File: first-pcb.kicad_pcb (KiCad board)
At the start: 2 copper layers, 88.9 x 45.7 mm, 8 parts, among them K1 my_connector, P1 10k, Q1 BC547, U1 LM358

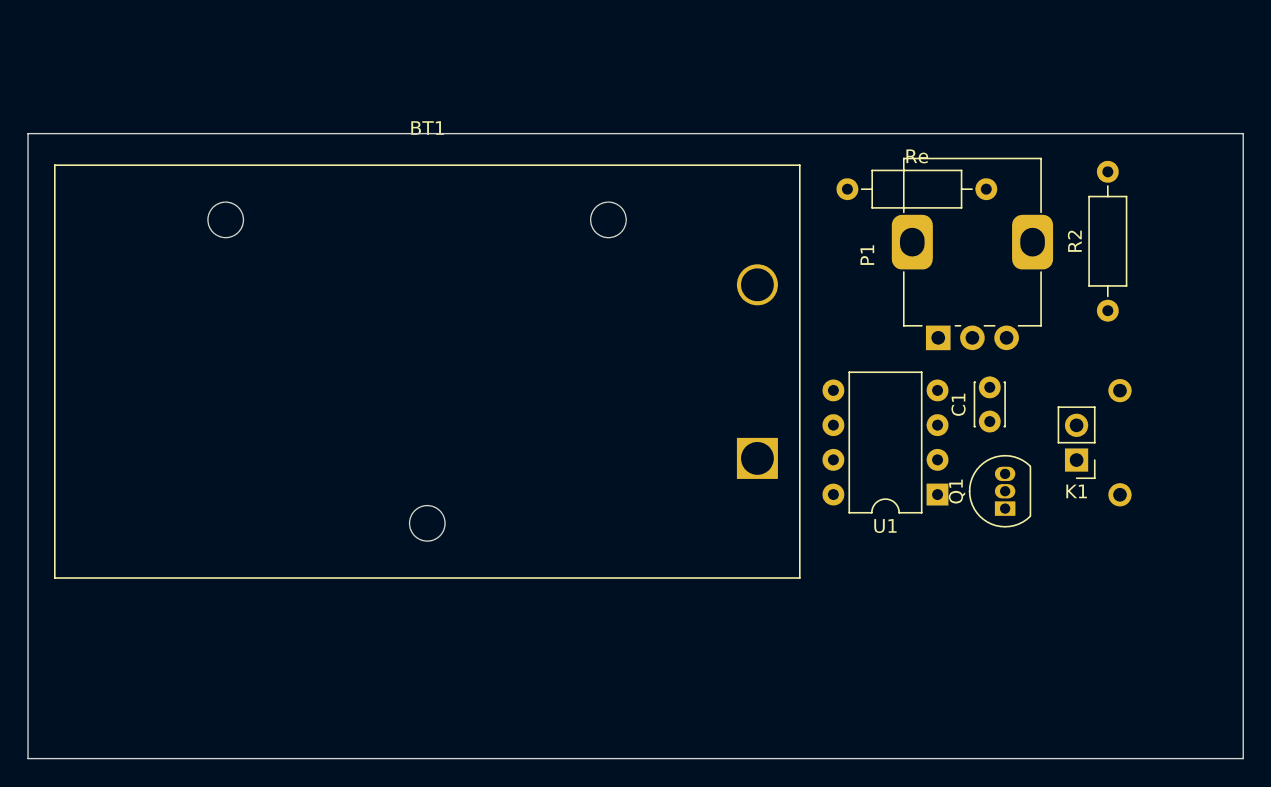
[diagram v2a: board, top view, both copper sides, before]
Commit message: Adding Grounding Holes to pcb
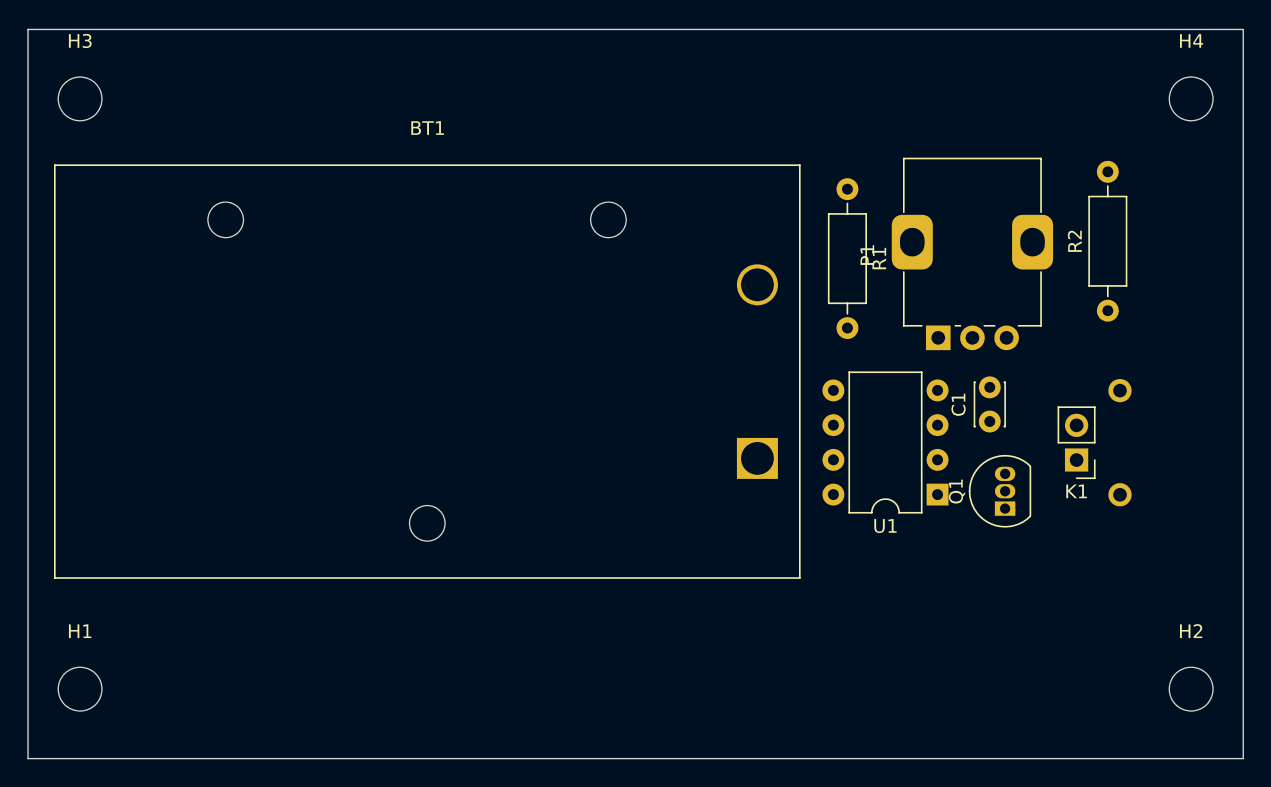
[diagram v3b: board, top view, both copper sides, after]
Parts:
- added H1: MountingHole_Pad, MountingHole:MountingHole_3.2mm_M3, F.Cu at (86.4, 119.4)
- added H2: MountingHole_Pad, MountingHole:MountingHole_3.2mm_M3, F.Cu at (167.6, 119.4)
- added H3: MountingHole_Pad, MountingHole:MountingHole_3.2mm_M3, F.Cu at (86.4, 76.2)
- added H4: MountingHole_Pad, MountingHole:MountingHole_3.2mm_M3, F.Cu at (167.6, 76.2)
- turned R1 to -90 degrees
- renumbered Re to R1
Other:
- board size 88.9 x 45.7 mm -> 88.9 x 53.3 mm
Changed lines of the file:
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@@
   (net 4 "GND")
   (net 5 "Net-(C1-Pad1)")
-  (net 6 "Net-(U1-Pad1)")
-  (net 7 "Net-(K1-Pad1)")
-  (net 8 "unconnected-(U1-Pad5)")
-  (net 9 "unconnected-(U1-Pad6)")
-  (net 10 "unconnected-(U1-Pad7)")
+  (net 6 "Net-(K1-Pad1)")
+  (net 7 "unconnected-(U1-Pad5)")
+  (net 8 "unconnected-(U1-Pad6)")
+  (net 9 "unconnected-(U1-Pad7)")
+  (net 10 "Net-(Q1-Pad2)")
   (footprint "Potentiometer_THT:Potentiometer_Alps_RK09K_Single_Vertical" (layer "F.Cu")
     (at 149.138 93.68 90)
@@
     (fp_line (start 6.985 8.89) (end 0.635 8.89) (layer "F.Fab") (width 0.1))
     (pad "1" thru_hole rect (at 0 0 180) (size 1.6 1.6) (drill 0.8) (layers *.Cu *.Mask)
-      (net 6 "Net-(U1-Pad1)") (pintype "output"))
+      (net 10 "Net-(Q1-Pad2)") (pintype "output"))
     (pad "2" thru_hole oval (at 0 2.54 180) (size 1.6 1.6) (drill 0.8) (layers *.Cu *.Mask)
-      (net 7 "Net-(K1-Pad1)") (pinfunction "-") (pintype "input"))
+      (net 6 "Net-(K1-Pad1)") (pinfunction "-") (pintype "input"))
     (pad "3" thru_hole oval (at 0 5.08 180) (size 1.6 1.6) (drill 0.8) (layers *.Cu *.Mask)
       (net 5 "Net-(C1-Pad1)") (pinfunction "+") (pintype "input"))
@@
       (net 4 "GND") (pinfunction "V-") (pintype "power_in"))
     (pad "5" thru_hole oval (at 7.62 7.62 180) (size 1.6 1.6) (drill 0.8) (layers *.Cu *.Mask)
-      (net 8 "unconnected-(U1-Pad5)") (pinfunction "+") (pintype "input+no_connect"))
+      (net 7 "unconnected-(U1-Pad5)") (pinfunction "+") (pintype "input+no_connect"))
     (pad "6" thru_hole oval (at 7.62 5.08 180) (size 1.6 1.6) (drill 0.8) (layers *.Cu *.Mask)
-      (net 9 "unconnected-(U1-Pad6)") (pinfunction "-") (pintype "input+no_connect"))
+      (net 8 "unconnected-(U1-Pad6)") (pinfunction "-") (pintype "input+no_connect"))
     (pad "7" thru_hole oval (at 7.62 2.54 180) (size 1.6 1.6) (drill 0.8) (layers *.Cu *.Mask)
-      (net 10 "unconnected-(U1-Pad7)") (pintype "output+no_connect"))
+      (net 9 "unconnected-(U1-Pad7)") (pintype "output+no_connect"))
     (pad "8" thru_hole oval (at 7.62 0 180) (size 1.6 1.6) (drill 0.8) (layers *.Cu *.Mask)
       (net 1 "Net-(BT1-Pad1)") (pinfunction "V+") (pintype "power_in"))
@@
       (rotate (xyz 0 0 0))
     )
+  )
+  (footprint "MountingHole:MountingHole_3.2mm_M3" (layer "F.Cu")
+    (at 86.36 76.2)
+    (descr "Mounting Hole 3.2mm, no annular, M3")
+    (tags "mounting hole 3.2mm no annular m3")
+    (property "Sheetfile" "first-pcb.kicad_sch")
+    (property "Sheetname" "")
+    (attr exclude_from_pos_files)
+    (fp_text reference "H3" (at 0 -4.2) (layer "F.SilkS")
+      (effects (font (size 1 1) (thickness 0.15)))
+    )
+    (fp_text value "MountingHole_Pad" (at 0 4.2) (layer "F.Fab")
+      (effects (font (size 1 1) (thickness 0.15)))
+    )
+    (fp_text user "${REFERENCE}" (at 0 0) (layer "F.Fab")
+      (effects (font (size 1 1) (thickness 0.15)))
+    )
+    (fp_circle (center 0 0) (end 3.2 0) (layer "Cmts.User") (width 0.15) (fill none))
+    (fp_circle (center 0 0) (end 3.45 0) (layer "F.CrtYd") (width 0.05) (fill none))
+    (pad "" np_thru_hole circle (at 0 0) (size 3.2 3.2) (drill 3.2) (layers *.Cu *.Mask))
+  )
+  (footprint "MountingHole:MountingHole_3.2mm_M3" (layer "F.Cu")
+    (at 86.36 119.38)
+    (descr "Mounting Hole 3.2mm, no annular, M3")
+    (tags "mounting hole 3.2mm no annular m3")
+    (property "Sheetfile" "first-pcb.kicad_sch")
+    (property "Sheetname" "")
+    (attr exclude_from_pos_files)
+    (fp_text reference "H1" (at 0 -4.2) (layer "F.SilkS")
+      (effects (font (size 1 1) (thickness 0.15)))
+    )
+    (fp_text value "MountingHole_Pad" (at 0 4.2) (layer "F.Fab")
+      (effects (font (size 1 1) (thickness 0.15)))
+    )
+    (fp_text user "${REFERENCE}" (at 0 0) (layer "F.Fab")
+      (effects (font (size 1 1) (thickness 0.15)))
+    )
+    (fp_circle (center 0 0) (end 3.2 0) (layer "Cmts.User") (width 0.15) (fill none))
+    (fp_circle (center 0 0) (end 3.45 0) (layer "F.CrtYd") (width 0.05) (fill none))
+    (pad "" np_thru_hole circle (at 0 0) (size 3.2 3.2) (drill 3.2) (layers *.Cu *.Mask))
   )
   (footprint "Battery:BatteryHolder_Eagle_12BH611-GR" (layer "F.Cu")
@@
       (net 1 "Net-(BT1-Pad1)") (pinfunction "C") (pintype "passive"))
     (pad "2" thru_hole oval (at 1.27 0 90) (size 1.05 1.5) (drill 0.75) (layers *.Cu *.Mask)
-      (net 6 "Net-(U1-Pad1)") (pinfunction "B") (pintype "input"))
+      (net 10 "Net-(Q1-Pad2)") (pinfunction "B") (pintype "input"))
     (pad "3" thru_hole oval (at 2.54 0 90) (size 1.05 1.5) (drill 0.75) (layers *.Cu *.Mask)
-      (net 7 "Net-(K1-Pad1)") (pinfunction "E") (pintype "passive"))
+      (net 6 "Net-(K1-Pad1)") (pinfunction "E") (pintype "passive"))
     (model "${KICAD6_3DMODEL_DIR}/Package_TO_SOT_THT.3dshapes/TO-92_Inline.wrl"
       (offset (xyz 0 0 0))
@@
   )
   (footprint "Resistor_THT:R_Axial_DIN0207_L6.3mm_D2.5mm_P10.16mm_Horizontal" (layer "F.Cu")
-    (at 142.494 82.804)
+    (at 142.494 82.804 -90)
     (descr "Resistor, Axial_DIN0207 series, Axial, Horizontal, pin pitch=10.16mm, 0.25W = 1/4W, length*diameter=6.3*2.5mm^2, http://cdn-reichelt.de/documents/datenblatt/B400/1_4W%23YAG.pdf")
     (tags "Resistor Axial_DIN0207 series Axial Horizontal pin pitch 10.16mm 0.25W = 1/4W length 6.3mm diameter 2.5mm")
@@
     (property "Sheetname" "")
     (attr through_hole)
-    (fp_text reference "Re" (at 5.08 -2.37) (layer "F.SilkS")
-      (effects (font (size 1 1) (thickness 0.15)))
-    )
-    (fp_text value "100R" (at 5.08 2.37) (layer "F.Fab")
-      (effects (font (size 1 1) (thickness 0.15)))
-    )
-    (fp_text user "${REFERENCE}" (at 5.08 0) (layer "F.Fab")
+    (fp_text reference "R1" (at 5.08 -2.37 90) (layer "F.SilkS")
+      (effects (font (size 1 1) (thickness 0.15)))
+    )
+    (fp_text value "100R" (at 5.08 2.37 90) (layer "F.Fab")
+      (effects (font (size 1 1) (thickness 0.15)))
+    )
+    (fp_text user "${REFERENCE}" (at 5.08 0 90) (layer "F.Fab")
       (effects (font (size 1 1) (thickness 0.15)))
     )
@@
     (fp_line (start 8.23 1.25) (end 8.23 -1.25) (layer "F.Fab") (width 0.1))
     (fp_line (start 1.93 1.25) (end 8.23 1.25) (layer "F.Fab") (width 0.1))
-    (pad "1" thru_hole circle (at 0 0) (size 1.6 1.6) (drill 0.8) (layers *.Cu *.Mask)
+    (pad "1" thru_hole circle (at 0 0 270) (size 1.6 1.6) (drill 0.8) (layers *.Cu *.Mask)
       (net 1 "Net-(BT1-Pad1)") (pintype "passive"))
-    (pad "2" thru_hole oval (at 10.16 0) (size 1.6 1.6) (drill 0.8) (layers *.Cu *.Mask)
+    (pad "2" thru_hole oval (at 10.16 0 270) (size 1.6 1.6) (drill 0.8) (layers *.Cu *.Mask)
       (net 2 "Net-(P1-Pad1)") (pintype "passive"))
     (model "${KICAD6_3DMODEL_DIR}/Resistor_THT.3dshapes/R_Axial_DIN0207_L6.3mm_D2.5mm_P10.16mm_Horizontal.wrl"
@@
     (fp_line (start -1.27 -0.635) (end -0.635 -1.27) (layer "F.Fab") (width 0.1))
     (pad "1" thru_hole rect (at 0 0 180) (size 1.7 1.7) (drill 1) (layers *.Cu *.Mask)
-      (net 7 "Net-(K1-Pad1)") (pintype "input"))
+      (net 6 "Net-(K1-Pad1)") (pintype "input"))
     (pad "2" thru_hole circle (at 0 2.54 180) (size 1.7 1.7) (drill 1) (layers *.Cu *.Mask)
       (net 4 "GND") (pintype "input"))
@@
       (rotate (xyz 0 0 0))
     )
+  )
+  (footprint "MountingHole:MountingHole_3.2mm_M3" (layer "F.Cu")
+    (at 167.64 119.38)
+    (descr "Mounting Hole 3.2mm, no annular, M3")
+    (tags "mounting hole 3.2mm no annular m3")
+    (property "Sheetfile" "first-pcb.kicad_sch")
+    (property "Sheetname" "")
+    (attr exclude_from_pos_files)
+    (fp_text reference "H2" (at 0 -4.2) (layer "F.SilkS")
+      (effects (font (size 1 1) (thickness 0.15)))
+    )
+    (fp_text value "MountingHole_Pad" (at 0 4.2) (layer "F.Fab")
+      (effects (font (size 1 1) (thickness 0.15)))
+    )
+    (fp_text user "${REFERENCE}" (at 0 0) (layer "F.Fab")
+      (effects (font (size 1 1) (thickness 0.15)))
+    )
+    (fp_circle (center 0 0) (end 3.2 0) (layer "Cmts.User") (width 0.15) (fill none))
+    (fp_circle (center 0 0) (end 3.45 0) (layer "F.CrtYd") (width 0.05) (fill none))
+    (pad "" np_thru_hole circle (at 0 0) (size 3.2 3.2) (drill 3.2) (layers *.Cu *.Mask))
   )
   (footprint "Capacitor_THT:C_Disc_D3.0mm_W2.0mm_P2.50mm" (layer "F.Cu")
@@
     )
   )
-  (gr_rect (start 82.55 124.46) (end 171.45 78.74) (layer "Edge.Cuts") (width 0.1) (fill none))
+  (footprint "MountingHole:MountingHole_3.2mm_M3" (layer "F.Cu")
+    (at 167.64 76.2)
+    (descr "Mounting Hole 3.2mm, no annular, M3")
+    (tags "mounting hole 3.2mm no annular m3")
+    (property "Sheetfile" "first-pcb.kicad_sch")
+    (property "Sheetname" "")
+    (attr exclude_from_pos_files)
+    (fp_text reference "H4" (at 0 -4.2) (layer "F.SilkS")
+      (effects (font (size 1 1) (thickness 0.15)))
+    )
+    (fp_text value "MountingHole_Pad" (at 0 4.2) (layer "F.Fab")
+      (effects (font (size 1 1) (thickness 0.15)))
+    )
+    (fp_text user "${REFERENCE}" (at 0 0) (layer "F.Fab")
+      (effects (font (size 1 1) (thickness 0.15)))
+    )
+    (fp_circle (center 0 0) (end 3.2 0) (layer "Cmts.User") (width 0.15) (fill none))
+    (fp_circle (center 0 0) (end 3.45 0) (layer "F.CrtYd") (width 0.05) (fill none))
+    (pad "" np_thru_hole circle (at 0 0) (size 3.2 3.2) (drill 3.2) (layers *.Cu *.Mask))
+  )
+  (gr_rect (start 82.55 124.46) (end 171.45 71.12) (layer "Edge.Cuts") (width 0.1) (fill none))
 )

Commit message: Routing
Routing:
- net GND: track 0.00 -> 54.2 mm, vias 0 -> 2
- net Net-(BT1-Pad1): track 0.00 -> 46.5 mm
- net Net-(C1-Pad1): track 0.00 -> 21.3 mm
- net Net-(K1-Pad1): track 0.00 -> 11.6 mm
- net Net-(P1-Pad3): track 0.00 -> 8.23 mm
- net Net-(P1-Pad1): track 0.00 -> 7.95 mm
- net Net-(Q1-Pad2): track 0.00 -> 5.04 mm
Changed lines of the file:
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@@
   )
   (gr_rect (start 82.55 124.46) (end 171.45 71.12) (layer "Edge.Cuts") (width 0.1) (fill none))
+  (segment (start 139.964 84.318) (end 141.478 82.804) (width 0.5) (layer "F.Cu") (net 1))
+  (segment (start 141.468 105.146) (end 141.468 107.178) (width 0.5) (layer "F.Cu") (net 1))
+  (segment (start 138.556 105.146) (end 135.91 102.5) (width 0.5) (layer "F.Cu") (net 1))
+  (segment (start 139.964 105.146) (end 138.556 105.146) (width 0.5) (layer "F.Cu") (net 1))
+  (segment (start 141.468 107.178) (end 142.494 108.204) (width 0.5) (layer "F.Cu") (net 1))
+  (segment (start 151.998 108.204) (end 154.03 106.172) (width 0.5) (layer "F.Cu") (net 1))
+  (segment (start 141.478 82.804) (end 142.494 82.804) (width 0.5) (layer "F.Cu") (net 1))
+  (segment (start 141.468 105.146) (end 139.964 105.146) (width 0.5) (layer "F.Cu") (net 1))
+  (segment (start 139.964 105.146) (end 139.964 84.318) (width 0.5) (layer "F.Cu") (net 1))
+  (segment (start 142.494 108.204) (end 151.998 108.204) (width 0.5) (layer "F.Cu") (net 1))
+  (segment (start 143.21 93.68) (end 149.138 93.68) (width 0.5) (layer "B.Cu") (net 2))
+  (segment (start 142.494 92.964) (end 143.21 93.68) (width 0.5) (layer "B.Cu") (net 2))
+  (segment (start 148.422 92.964) (end 149.138 93.68) (width 0.25) (layer "B.Cu") (net 2))
+  (segment (start 154.138 93.68) (end 159.558 93.68) (width 0.5) (layer "B.Cu") (net 3))
+  (segment (start 159.558 93.68) (end 161.544 91.694) (width 0.5) (layer "B.Cu") (net 3))
+  (segment (start 135.91 93.746) (end 137.16 94.996) (width 0.5) (layer "F.Cu") (net 4))
+  (segment (start 135.91 89.8) (end 135.91 93.746) (width 0.5) (layer "F.Cu") (net 4))
+  (segment (start 159.258 83.82) (end 161.544 81.534) (width 0.5) (layer "F.Cu") (net 4))
+  (segment (start 149.088 97.526) (end 150.3205 97.526) (width 0.5) (layer "F.Cu") (net 4))
+  (segment (start 159.258 100.081) (end 159.258 83.82) (width 0.5) (layer "F.Cu") (net 4))
+  (segment (start 150.3205 97.526) (end 150.3305 97.536) (width 0.5) (layer "F.Cu") (net 4))
+  (via (at 137.16 94.996) (size 0.8) (drill 0.4) (layers "F.Cu" "B.Cu") (net 4))
+  (via (at 150.3305 97.536) (size 0.8) (drill 0.4) (layers "F.Cu" "B.Cu") (net 4))
+  (segment (start 149.088 97.526) (end 149.088 97.678366) (width 0.5) (layer "B.Cu") (net 4))
+  (segment (start 152.674 97.536) (end 152.908 97.302) (width 0.5) (layer "B.Cu") (net 4))
+  (segment (start 137.16 94.996) (end 146.558 94.996) (width 0.5) (layer "B.Cu") (net 4))
+  (segment (start 149.088 97.678366) (end 152.411145 101.001511) (width 0.5) (layer "B.Cu") (net 4))
+  (segment (start 152.411145 101.001511) (end 158.337489 101.001511) (width 0.5) (layer "B.Cu") (net 4))
+  (segment (start 146.558 94.996) (end 149.088 97.526) (width 0.5) (layer "B.Cu") (net 4))
+  (segment (start 158.337489 101.001511) (end 159.258 100.081) (width 0.5) (layer "B.Cu") (net 4))
+  (segment (start 150.3305 97.536) (end 152.674 97.536) (width 0.5) (layer "B.Cu") (net 4))
+  (segment (start 152.644 100.066) (end 152.908 99.802) (width 0.5) (layer "F.Cu") (net 5))
+  (segment (start 149.088 100.066) (end 152.644 100.066) (width 0.5) (layer "F.Cu") (net 5))
+  (segment (start 149.616 100.066) (end 151.13 98.552) (width 0.5) (layer "F.Cu") (net 5))
+  (segment (start 151.13 94.188) (end 151.638 93.68) (width 0.5) (layer "F.Cu") (net 5))
+  (segment (start 149.088 100.066) (end 149.616 100.066) (width 0.5) (layer "F.Cu") (net 5))
+  (segment (start 151.13 98.552) (end 151.13 94.188) (width 0.5) (layer "F.Cu") (net 5))
+  (segment (start 151.638 93.68) (end 153.462 95.504) (width 0.5) (layer "B.Cu") (net 5))
+  (segment (start 154.94 96.012) (end 154.94 99.06) (width 0.5) (layer "B.Cu") (net 5))
+  (segment (start 154.94 99.06) (end 154.198 99.802) (width 0.5) (layer "B.Cu") (net 5))
+  (segment (start 154.432 95.504) (end 154.94 96.012) (width 0.5) (layer "B.Cu") (net 5))
+  (segment (start 154.198 99.802) (end 152.908 99.802) (width 0.5) (layer "B.Cu") (net 5))
+  (segment (start 153.462 95.504) (end 154.432 95.504) (width 0.5) (layer "B.Cu") (net 5))
+  (segment (start 153.004 102.606) (end 154.03 103.632) (width 0.5) (layer "F.Cu") (net 6))
+  (segment (start 149.088 102.606) (end 153.004 102.606) (width 0.5) (layer "F.Cu") (net 6))
+  (segment (start 153.004 102.606) (end 153.019 102.621) (width 0.5) (layer "F.Cu") (net 6))
+  (segment (start 153.019 102.621) (end 159.258 102.621) (width 0.5) (layer "F.Cu") (net 6))
+  (segment (start 153.786 105.146) (end 154.03 104.902) (width 0.5) (layer "F.Cu") (net 10))
+  (segment (start 149.088 105.146) (end 153.786 105.146) (width 0.5) (layer "F.Cu") (net 10))
 )
